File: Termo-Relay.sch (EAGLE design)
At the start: 50 parts, among them CN1 PBS-2-VERTICAL, CN2 PBS-2-VERTICAL, CN3 PBS-2-VERTICAL, CN5 PBS-4-VERTICAL, IC1 74HCT595D, IC2 74HCT595D, IC3 STM8S103FP, Q2 16M, T1 2N2222, T2 2N2222, T3 2N2222, T4 2N2222

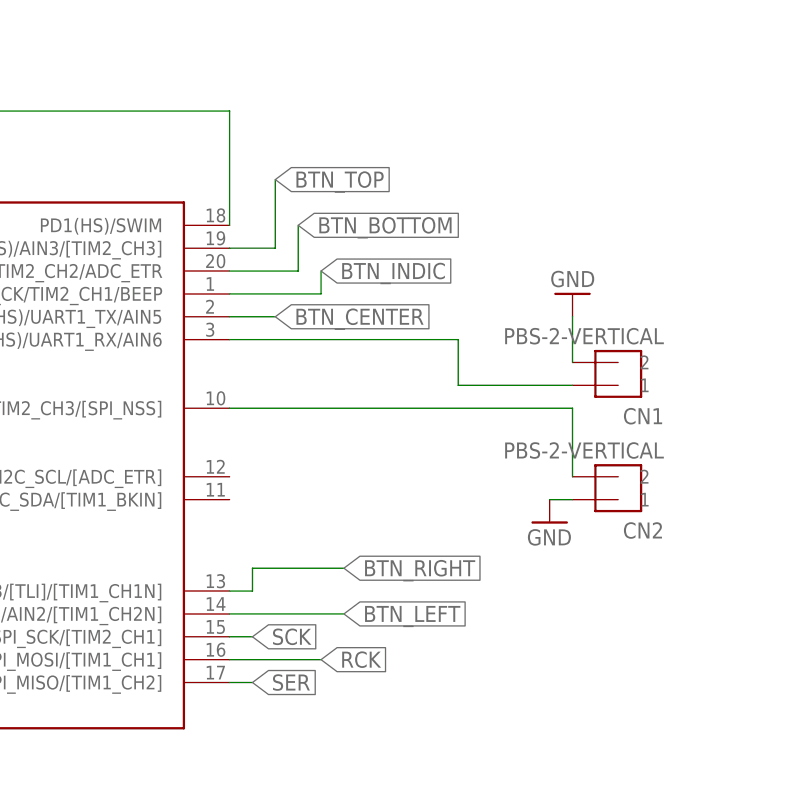
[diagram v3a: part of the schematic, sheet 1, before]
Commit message: Roads for buttons and power were added. One error (center button was not connected to STM) was corrected
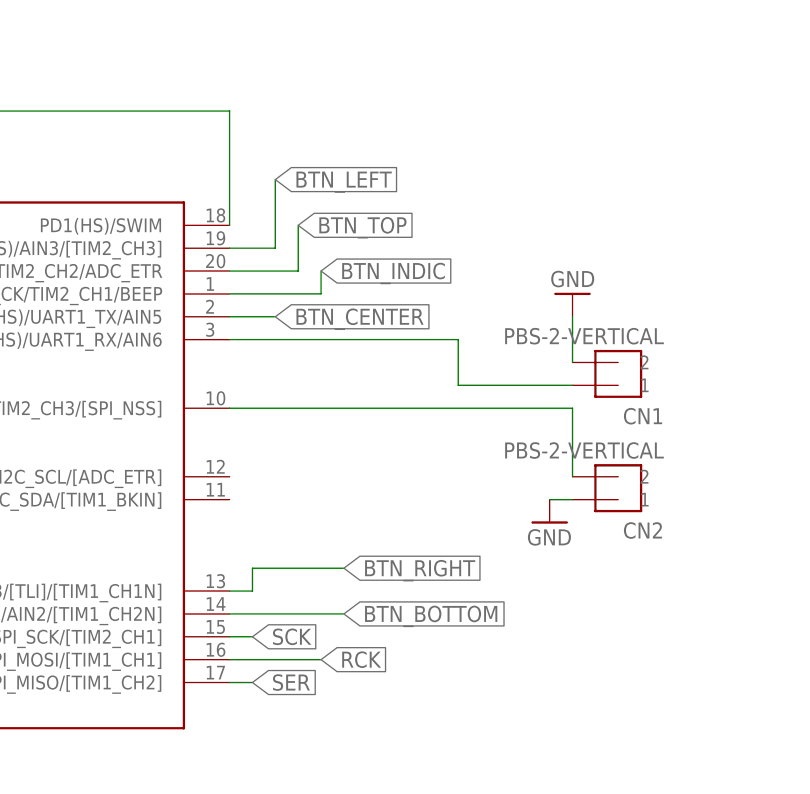
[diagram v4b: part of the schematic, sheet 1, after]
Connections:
- net BTN_BOTTOM: now also IC3.PC4(HS)/TIM1_CH4/CLK_CCO/AIN2/[TIM1_CH2N]; no longer IC3.PD3(HS)/AIN4/TIM2_CH2/ADC_ETR
- net BTN_CENTER: now also IC3.PD5(HS)/UART1_TX/AIN5
- net BTN_LEFT: now also IC3.PD2(HS)/AIN3/[TIM2_CH3]; no longer IC3.PC4(HS)/TIM1_CH4/CLK_CCO/AIN2/[TIM1_CH2N]
- net BTN_TOP: now also IC3.PD3(HS)/AIN4/TIM2_CH2/ADC_ETR; no longer IC3.PD2(HS)/AIN3/[TIM2_CH3]
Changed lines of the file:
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@@
 </segment>
 <segment>
-<wire x1="63.5" y1="66.04" x2="76.2" y2="66.04" width="0.1524" layer="91"/>
-<label x="76.2" y="66.04" size="1.778" layer="95" xref="yes"/>
-<pinref part="IC3" gate="G$1" pin="PC4(HS)/TIM1_CH4/CLK_CCO/AIN2/[TIM1_CH2N]"/>
+<label x="68.58" y="114.3" size="1.778" layer="95" xref="yes"/>
+<pinref part="IC3" gate="G$1" pin="PD2(HS)/AIN3/[TIM2_CH3]"/>
+<wire x1="63.5" y1="106.68" x2="68.58" y2="106.68" width="0.1524" layer="91"/>
+<wire x1="68.58" y1="106.68" x2="68.58" y2="114.3" width="0.1524" layer="91"/>
 </segment>
 </net>
@@
 <wire x1="63.5" y1="99.06" x2="68.58" y2="99.06" width="0.1524" layer="91"/>
 <label x="68.58" y="99.06" size="1.778" layer="95" xref="yes"/>
+<pinref part="IC3" gate="G$1" pin="PD5(HS)/UART1_TX/AIN5"/>
 </segment>
 </net>
@@
 </segment>
 <segment>
-<wire x1="63.5" y1="104.14" x2="71.12" y2="104.14" width="0.1524" layer="91"/>
-<wire x1="71.12" y1="104.14" x2="71.12" y2="109.22" width="0.1524" layer="91"/>
-<label x="71.12" y="109.22" size="1.778" layer="95" xref="yes"/>
-<pinref part="IC3" gate="G$1" pin="PD3(HS)/AIN4/TIM2_CH2/ADC_ETR"/>
+<wire x1="63.5" y1="66.04" x2="76.2" y2="66.04" width="0.1524" layer="91"/>
+<label x="76.2" y="66.04" size="1.778" layer="95" xref="yes"/>
+<pinref part="IC3" gate="G$1" pin="PC4(HS)/TIM1_CH4/CLK_CCO/AIN2/[TIM1_CH2N]"/>
 </segment>
 </net>
@@
 </segment>
 <segment>
-<label x="68.58" y="114.3" size="1.778" layer="95" xref="yes"/>
-<pinref part="IC3" gate="G$1" pin="PD2(HS)/AIN3/[TIM2_CH3]"/>
-<wire x1="63.5" y1="106.68" x2="68.58" y2="106.68" width="0.1524" layer="91"/>
-<wire x1="68.58" y1="106.68" x2="68.58" y2="114.3" width="0.1524" layer="91"/>
+<wire x1="63.5" y1="104.14" x2="71.12" y2="104.14" width="0.1524" layer="91"/>
+<wire x1="71.12" y1="104.14" x2="71.12" y2="109.22" width="0.1524" layer="91"/>
+<label x="71.12" y="109.22" size="1.778" layer="95" xref="yes"/>
+<pinref part="IC3" gate="G$1" pin="PD3(HS)/AIN4/TIM2_CH2/ADC_ETR"/>
 </segment>
 </net>
